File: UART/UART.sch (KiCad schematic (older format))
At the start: 56 parts, among them J1 USB_B_Mini, J2 Conn_01x06, U1 FT232H, U2 93CxxB, U3 AZ1117-3.3, Y1 12MHz

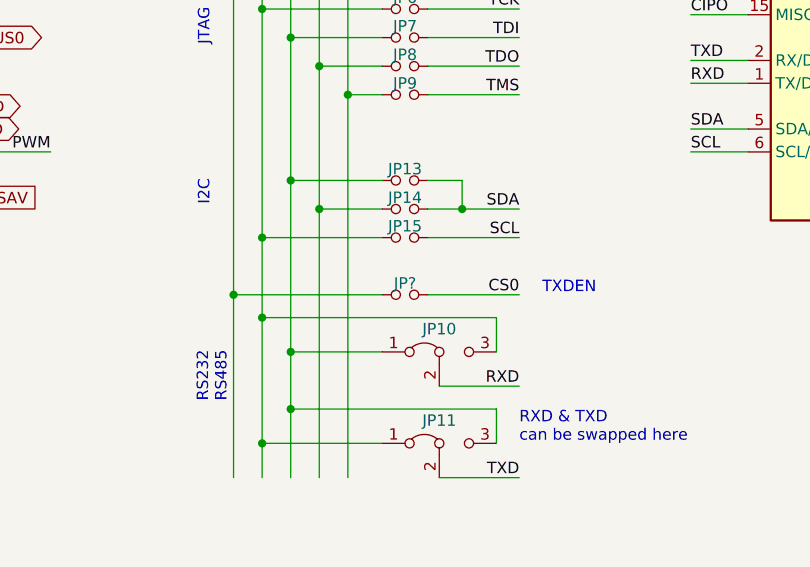
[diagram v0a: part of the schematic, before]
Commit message: fix some ERC/DRC
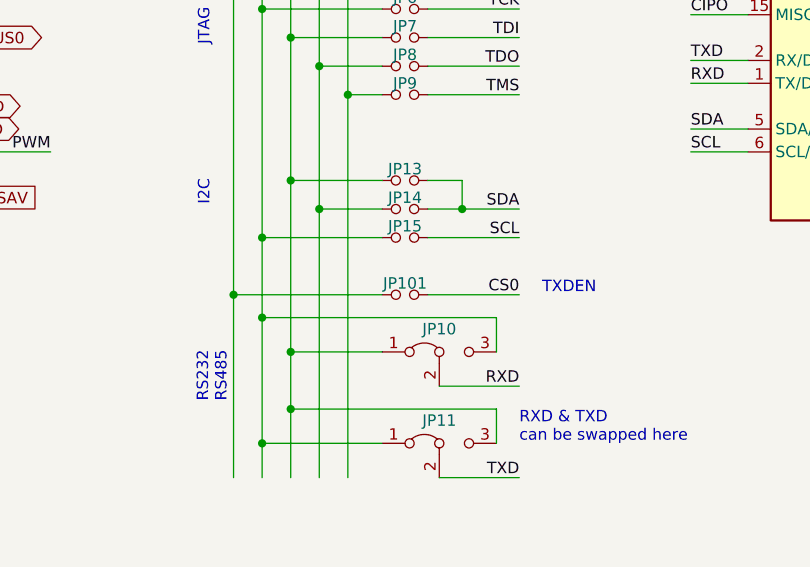
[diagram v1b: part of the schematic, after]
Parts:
- gave numbers to parts that had none: 1
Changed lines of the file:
@@
 	6750 2500 6750 4625
 $Comp
-L Device:Jumper_NO_Small JP?
+L Device:Jumper_NO_Small JP101
 U 1 1 60A14634
 P 7500 4625
-F 0 "JP?" H 7500 4675 50  0000 C CNN
+F 0 "JP101" H 7500 4675 50  0000 C CNN
 F 1 "Jumper_NO_Small" H 7525 4725 50  0001 C CNN
 F 2 "Jumper:SolderJumper-2_P1.3mm_Open_RoundedPad1.0x1.5mm" H 7500 4625 50  0001 C CNN
